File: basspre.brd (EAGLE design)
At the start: 38.8 x 28.7 mm, 27 parts, among them U1 LM4250, U101 TLE2426IDR, U103 LM4250

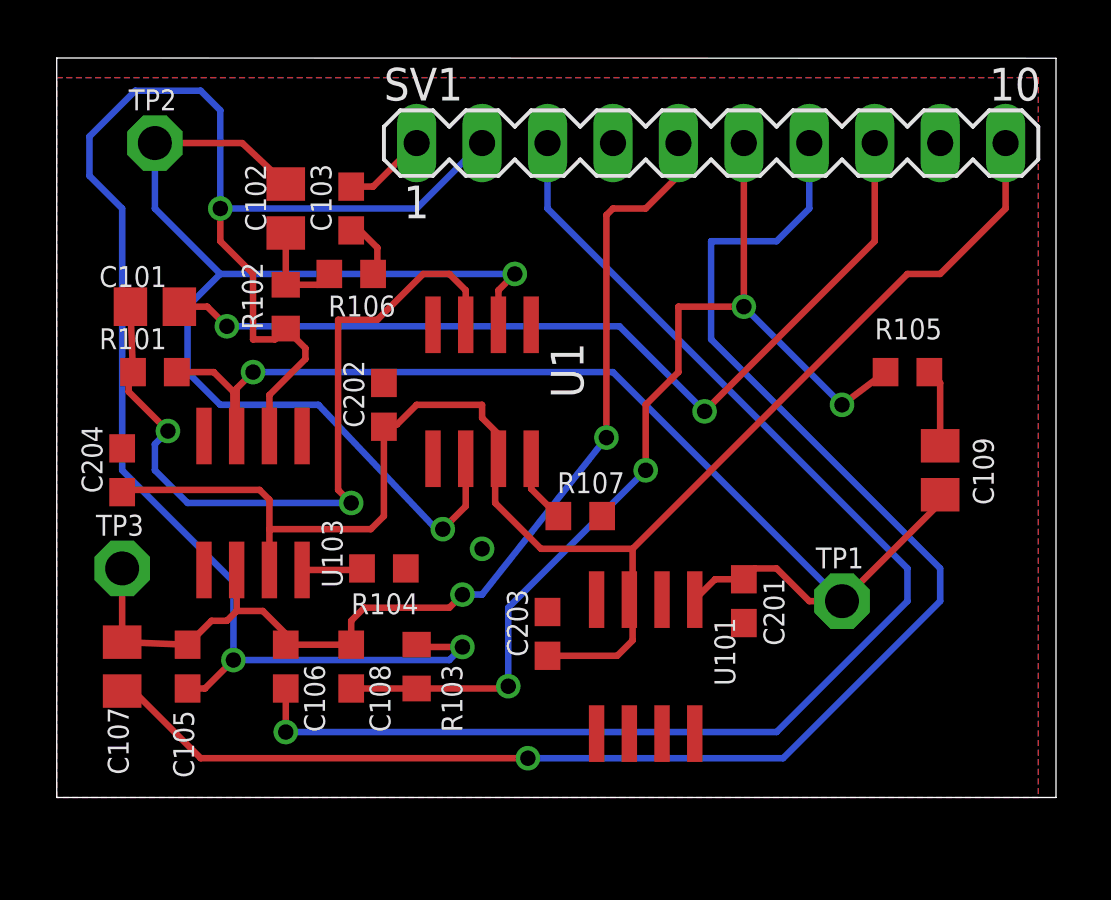
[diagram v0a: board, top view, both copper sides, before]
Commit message: redid layout to be smaller
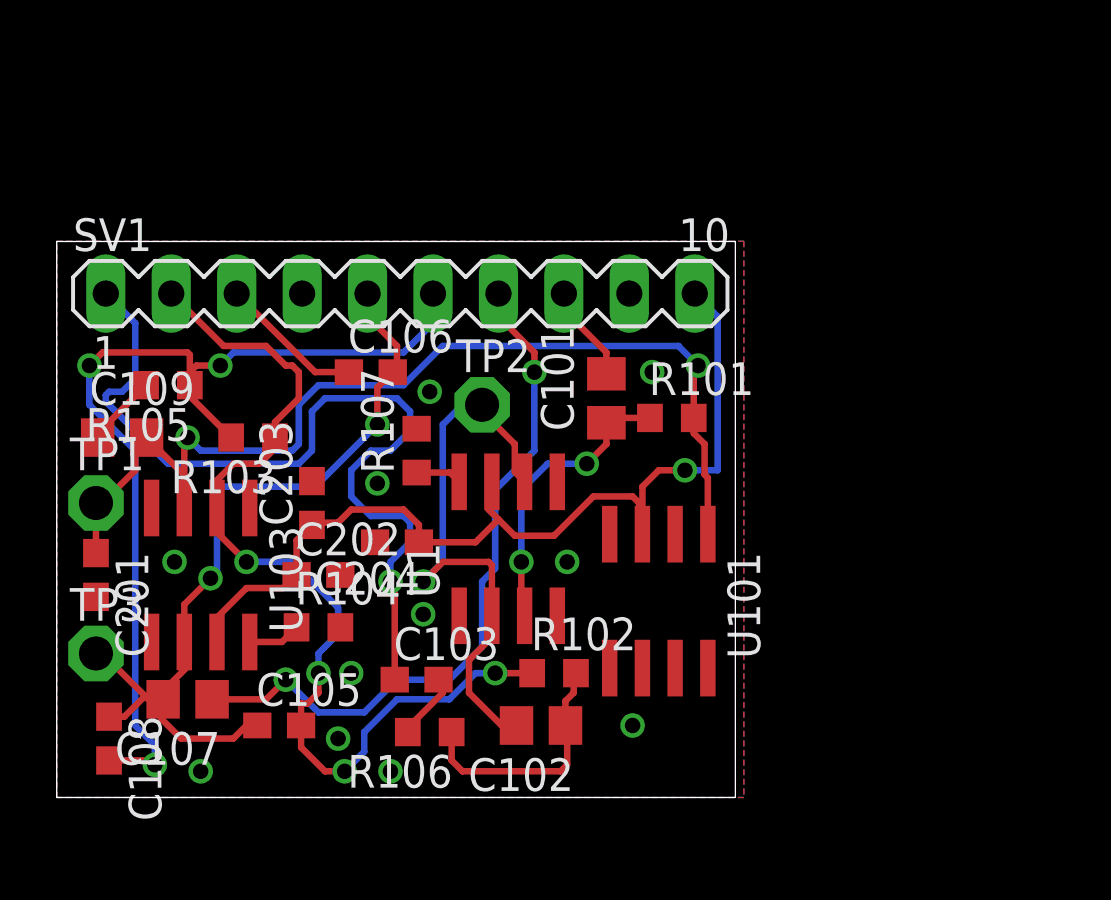
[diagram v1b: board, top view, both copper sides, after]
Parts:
- removed U$1: (no value), SparkFun:OSHW-LOGO-L
- moved C109 31.8 mm to (2.54, 14.0), turned to 0 degrees
- moved TP1 29.2 mm to (1.52, 11.4)
- moved R105 28.7 mm to (4.32, 16.0), turned to 180 degrees
- moved C201 25.2 mm to (1.52, 8.64)
- moved C102 22.4 mm to (18.8, 2.79), turned to 180 degrees
- moved R101 20.1 mm to (23.9, 14.7)
- moved C103 18.5 mm to (14.0, 4.57), turned to 0 degrees
- moved R106 18.0 mm to (14.5, 2.54), turned to 180 degrees
- moved C101 17.9 mm to (21.3, 15.5), turned to 90 degrees
- moved R102 17.6 mm to (19.3, 4.83), turned to 0 degrees
- moved TP2 16.3 mm to (16.5, 15.2)
- moved SV1 13.4 mm to (13.3, 19.6)
- moved C106 11.9 mm to (12.2, 16.5), turned to 0 degrees
- moved C204 11.0 mm to (13.2, 9.91), turned to 180 degrees
- moved R103 10.9 mm to (7.62, 14.0), turned to 180 degrees
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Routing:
- net TREBLE1: track 51.5 -> 5.62 mm, vias 1 -> 0
- net OUTPUT: track 59.9 -> 27.5 mm, vias 1 -> 2
- net INPUT: track 35.2 -> 3.90 mm, vias 2 -> 0
- net TREBLE2: track 69.1 -> 37.9 mm, vias 3 -> 4
- net TREBLE3: track 3.24 -> 34.3 mm, vias 0 -> 1
- net V+: track 60.9 -> 37.3 mm, vias 0 -> 1
- net N$3: track 45.5 -> 22.6 mm, vias 2 -> 1
- net C1: track 30.0 -> 11.6 mm
- net BASS2: track 42.2 -> 32.5 mm
- net VGND: track 46.0 -> 40.1 mm, vias 1 -> 2
- net N$1: track 3.87 -> 9.62 mm
- net BASS1: track 40.0 -> 37.8 mm, vias 4 -> 3
- net R107: track 2.66 -> 1.80 mm
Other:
- board size 38.8 x 28.7 mm -> 26.3 x 21.6 mm
- board text removed: "BASSPRE-MM2 ALPHA"
- board text removed: "CC-BY-SA"
- board text removed: "github.com/russellmcc"

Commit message: added labeling silkscreens
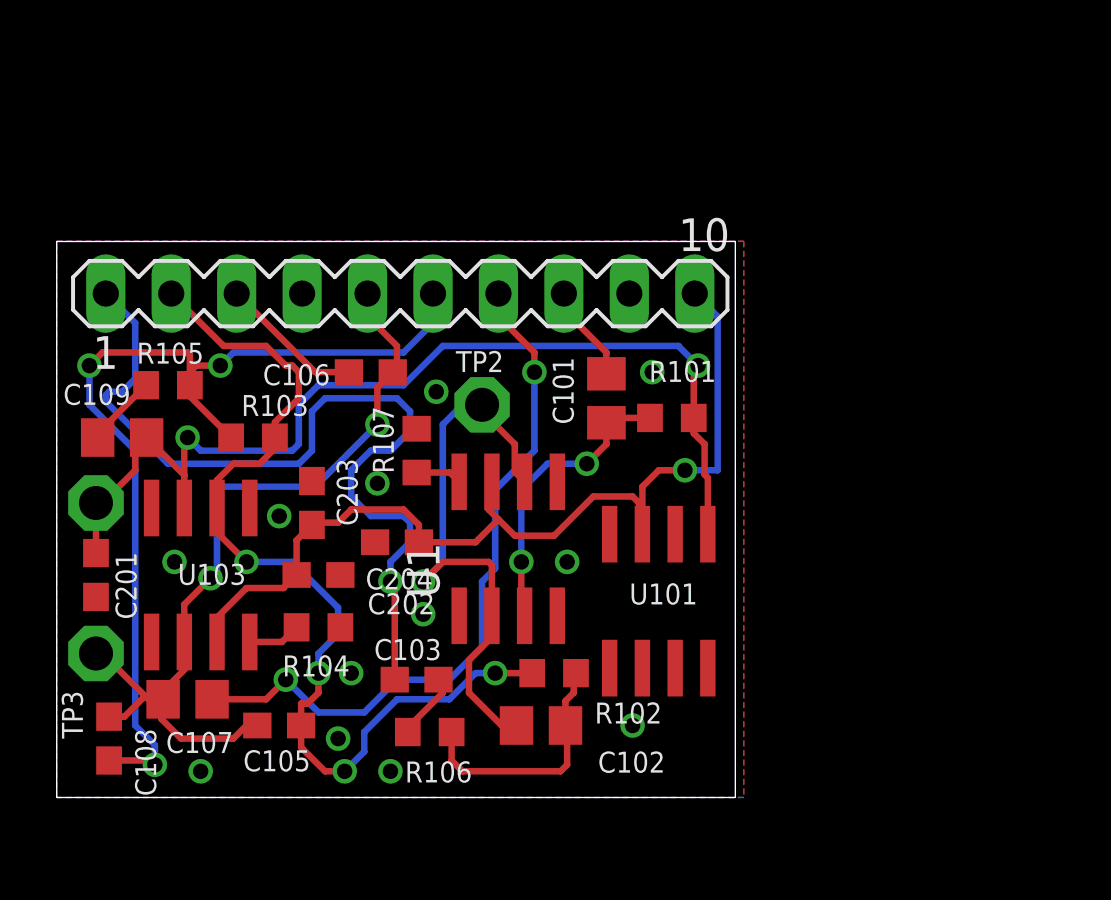
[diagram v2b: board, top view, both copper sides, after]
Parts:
- added U$1: (no value), SparkFun:OSHW-LOGO-L
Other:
- board text added: "(c) 2014 CC-BY-SA"
- board text added: "BASSPRE-MM2 ALPHA"
- board text added: "github.com/russellmcc"
